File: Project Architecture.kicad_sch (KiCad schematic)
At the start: 0 parts

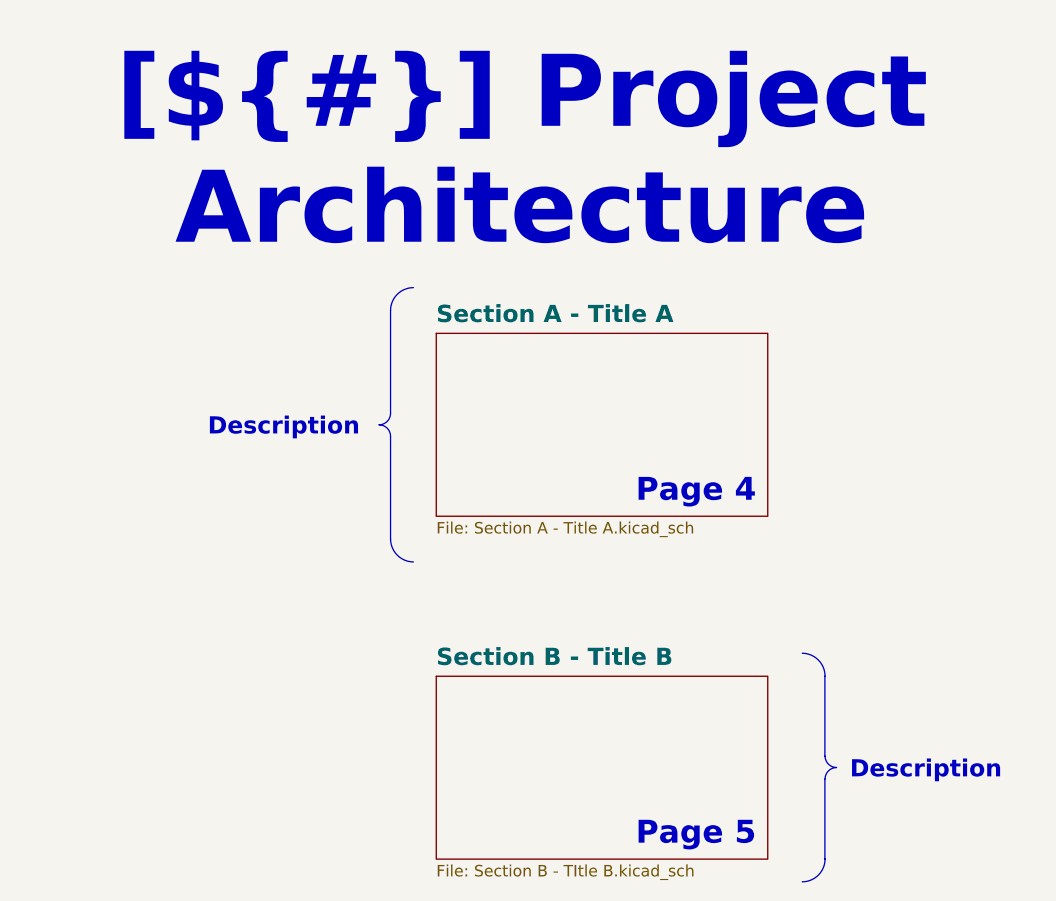
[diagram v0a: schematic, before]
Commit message: Progress on Block Diagram
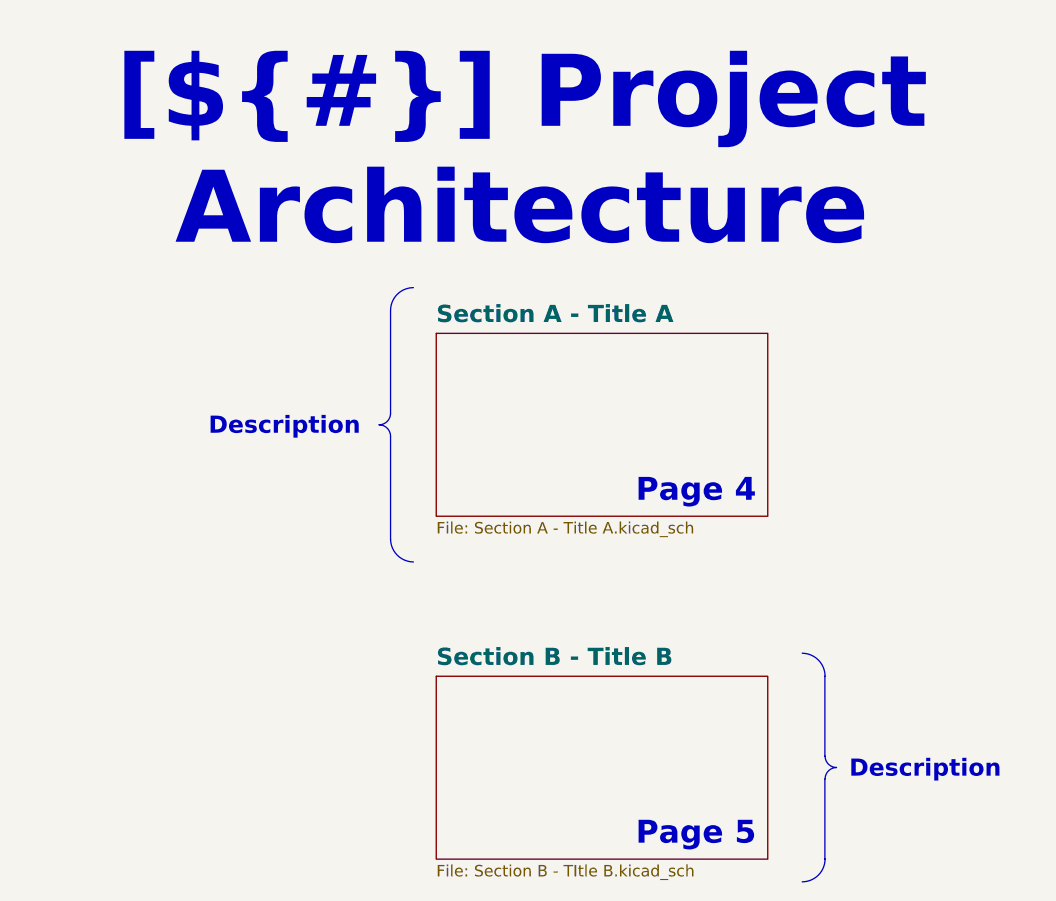
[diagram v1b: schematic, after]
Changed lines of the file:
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@@
 (kicad_sch
-	(version 20231120)
+	(version 20250114)
 	(generator "eeschema")
-	(generator_version "8.0")
+	(generator_version "9.0")
 	(paper "A3")
 	(title_block
@@
 		(company "${COMPANY}")
 	)
+	(arc
+		(start 243.86 96.5)
+		(mid 244.2349 95.6049)
+		(end 245.13 95.23)
+		(stroke
+			(width 0)
+			(type default)
+		)
+		(fill
+			(type none)
+		)
+	)
+	(arc
+		(start 195.58 55.88)
+		(mid 195.2051 56.7751)
+		(end 194.31 57.15)
+		(stroke
+			(width 0)
+			(type default)
+		)
+		(fill
+			(type none)
+		)
+	)
+	(arc
+		(start 241.32 82.53)
+		(mid 243.1102 83.2798)
+		(end 243.86 85.07)
+		(stroke
+			(width 0)
+			(type default)
+		)
+		(fill
+			(type none)
+		)
+	)
+	(arc
+		(start 194.31 57.15)
+		(mid 195.2051 57.5249)
+		(end 195.58 58.42)
+		(stroke
+			(width 0)
+			(type default)
+		)
+		(fill
+			(type none)
+		)
+	)
+	(arc
+		(start 243.86 105.39)
+		(mid 243.1161 107.1861)
+		(end 241.32 107.93)
+		(stroke
+			(width 0)
+			(type default)
+		)
+		(fill
+			(type none)
+		)
+	)
+	(arc
+		(start 245.13 95.23)
+		(mid 244.2349 94.8551)
+		(end 243.86 93.96)
+		(stroke
+			(width 0)
+			(type default)
+		)
+		(fill
+			(type none)
+		)
+	)
+	(arc
+		(start 195.58 44.45)
+		(mid 196.3239 42.6539)
+		(end 198.12 41.91)
+		(stroke
+			(width 0)
+			(type default)
+		)
+		(fill
+			(type none)
+		)
+	)
+	(arc
+		(start 198.12 72.39)
+		(mid 196.3298 71.6402)
+		(end 195.58 69.85)
+		(stroke
+			(width 0)
+			(type default)
+		)
+		(fill
+			(type none)
+		)
+	)
+	(text "Page 4"
+		(exclude_from_sim no)
+		(at 236.22 66.04 0)
+		(effects
+			(font
+				(size 2.54 2.54)
+				(bold yes)
+				(color 20 60 40 1)
+			)
+			(justify right bottom)
+			(href "#4")
+		)
+	)
+	(text "Page 5"
+		(exclude_from_sim no)
+		(at 236.22 104.14 0)
+		(effects
+			(font
+				(size 2.54 2.54)
+				(bold yes)
+				(color 100 70 50 1)
+			)
+			(justify right bottom)
+			(href "#5")
+		)
+	)
+	(text_box "Description"
+		(exclude_from_sim no)
+		(at 176.53 54.61 0)
+		(size 17.145 5.08)
+		(margins 1.4287 1.4287 1.4287 1.4287)
+		(stroke
+			(width -0.0001)
+			(type default)
+		)
+		(fill
+			(type none)
+		)
+		(effects
+			(font
+				(size 1.905 1.905)
+				(thickness 0.381)
+				(bold yes)
+				(color 0 0 0 1)
+			)
+			(justify right top)
+		)
+	)
+	(text_box "[${#}] ${TITLE}"
+		(exclude_from_sim no)
+		(at 144.78 20.32 0)
+		(size 130.81 12.7)
+		(margins 5.9999 5.9999 5.9999 5.9999)
+		(stroke
+			(width -0.0001)
+			(type default)
+		)
+		(fill
+			(type none)
+		)
+		(effects
+			(font
+				(face "Times New Roman")
+				(size 8 8)
+				(thickness 1.2)
+				(bold yes)
+				(color 162 22 34 1)
+			)
+		)
+	)
+	(text_box "Description"
+		(exclude_from_sim no)
+		(at 245.11 92.71 0)
+		(size 26.015 5.1)
+		(margins 1.4287 1.4287 1.4287 1.4287)
+		(stroke
+			(width -0.0001)
+			(type default)
+		)
+		(fill
+			(type none)
+		)
+		(effects
+			(font
+				(size 1.905 1.905)
+				(thickness 0.381)
+				(bold yes)
+				(color 0 0 0 1)
+			)
+			(justify left top)
+		)
+	)
 	(polyline
 		(pts
@@
 		)
 	)
-	(arc
-		(start 243.86 96.5)
-		(mid 244.2349 95.6049)
-		(end 245.13 95.23)
-		(stroke
-			(width 0)
-			(type default)
-		)
-		(fill
-			(type none)
-		)
-	)
-	(arc
-		(start 195.58 55.88)
-		(mid 195.2051 56.7751)
-		(end 194.31 57.15)
-		(stroke
-			(width 0)
-			(type default)
-		)
-		(fill
-			(type none)
-		)
-	)
-	(arc
-		(start 241.32 82.53)
-		(mid 243.1102 83.2798)
-		(end 243.86 85.07)
-		(stroke
-			(width 0)
-			(type default)
-		)
-		(fill
-			(type none)
-		)
-	)
-	(arc
-		(start 194.31 57.15)
-		(mid 195.2051 57.5249)
-		(end 195.58 58.42)
-		(stroke
-			(width 0)
-			(type default)
-		)
-		(fill
-			(type none)
-		)
-	)
-	(arc
-		(start 243.86 105.39)
-		(mid 243.1161 107.1861)
-		(end 241.32 107.93)
-		(stroke
-			(width 0)
-			(type default)
-		)
-		(fill
-			(type none)
-		)
-	)
-	(arc
-		(start 245.13 95.23)
-		(mid 244.2349 94.8551)
-		(end 243.86 93.96)
-		(stroke
-			(width 0)
-			(type default)
-		)
-		(fill
-			(type none)
-		)
-	)
-	(arc
-		(start 195.58 44.45)
-		(mid 196.3239 42.6539)
-		(end 198.12 41.91)
-		(stroke
-			(width 0)
-			(type default)
-		)
-		(fill
-			(type none)
-		)
-	)
-	(arc
-		(start 198.12 72.39)
-		(mid 196.3298 71.6402)
-		(end 195.58 69.85)
-		(stroke
-			(width 0)
-			(type default)
-		)
-		(fill
-			(type none)
-		)
-	)
-	(text_box "Description"
-		(exclude_from_sim no)
-		(at 176.53 54.61 0)
-		(size 17.145 5.08)
-		(stroke
-			(width -0.0001)
-			(type default)
-		)
-		(fill
-			(type none)
-		)
-		(effects
-			(font
-				(size 1.905 1.905)
-				(thickness 0.381)
-				(bold yes)
-				(color 0 0 0 1)
-			)
-			(justify right top)
-		)
-	)
-	(text_box "[${#}] ${TITLE}"
-		(exclude_from_sim no)
-		(at 144.78 20.32 0)
-		(size 130.81 12.7)
-		(stroke
-			(width -0.0001)
-			(type default)
-		)
-		(fill
-			(type none)
-		)
-		(effects
-			(font
-				(face "Times New Roman")
-				(size 8 8)
-				(thickness 1.2)
-				(bold yes)
-				(color 162 22 34 1)
-			)
-		)
-	)
-	(text_box "Description"
-		(exclude_from_sim no)
-		(at 245.11 92.71 0)
-		(size 26.015 5.1)
-		(stroke
-			(width -0.0001)
-			(type default)
-		)
-		(fill
-			(type none)
-		)
-		(effects
-			(font
-				(size 1.905 1.905)
-				(thickness 0.381)
-				(bold yes)
-				(color 0 0 0 1)
-			)
-			(justify left top)
-		)
-	)
-	(text "Page 4"
-		(exclude_from_sim no)
-		(at 236.22 66.04 0)
-		(effects
-			(font
-				(size 2.54 2.54)
-				(bold yes)
-				(color 20 60 40 1)
-			)
-			(justify right bottom)
-			(href "#4")
-		)
-	)
-	(text "Page 5"
-		(exclude_from_sim no)
-		(at 236.22 104.14 0)
-		(effects
-			(font
-				(size 2.54 2.54)
-				(bold yes)
-				(color 100 70 50 1)
-			)
-			(justify right bottom)
-			(href "#5")
-		)
-	)
 	(sheet
 		(at 200.66 46.99)
 		(size 36.83 20.32)
+		(exclude_from_sim no)
+		(in_bom yes)
+		(on_board yes)
+		(dnp no)
 		(fields_autoplaced yes)
 		(stroke
@@
 		)
 		(instances
-			(project "KDT_Hierarchical"
+			(project "CM5 Nas"
 				(path "/0650c7a8-acba-429c-9f8e-eec0baf0bc1c/fede4c36-00cc-4d3d-b71c-5243ba232202"
 					(page "4")
@@
 		(at 200.66 85.09)
 		(size 36.83 20.32)
+		(exclude_from_sim no)
+		(in_bom yes)
+		(on_board yes)
+		(dnp no)
 		(fields_autoplaced yes)
 		(stroke
@@
 		)
 		(instances
-			(project "KDT_Hierarchical"
+			(project "CM5 Nas"
 				(path "/0650c7a8-acba-429c-9f8e-eec0baf0bc1c/fede4c36-00cc-4d3d-b71c-5243ba232202"
 					(page "5")
